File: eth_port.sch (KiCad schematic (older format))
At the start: 48 parts, among them J301 8P8C_LED_Shielded, U301 LAN8810

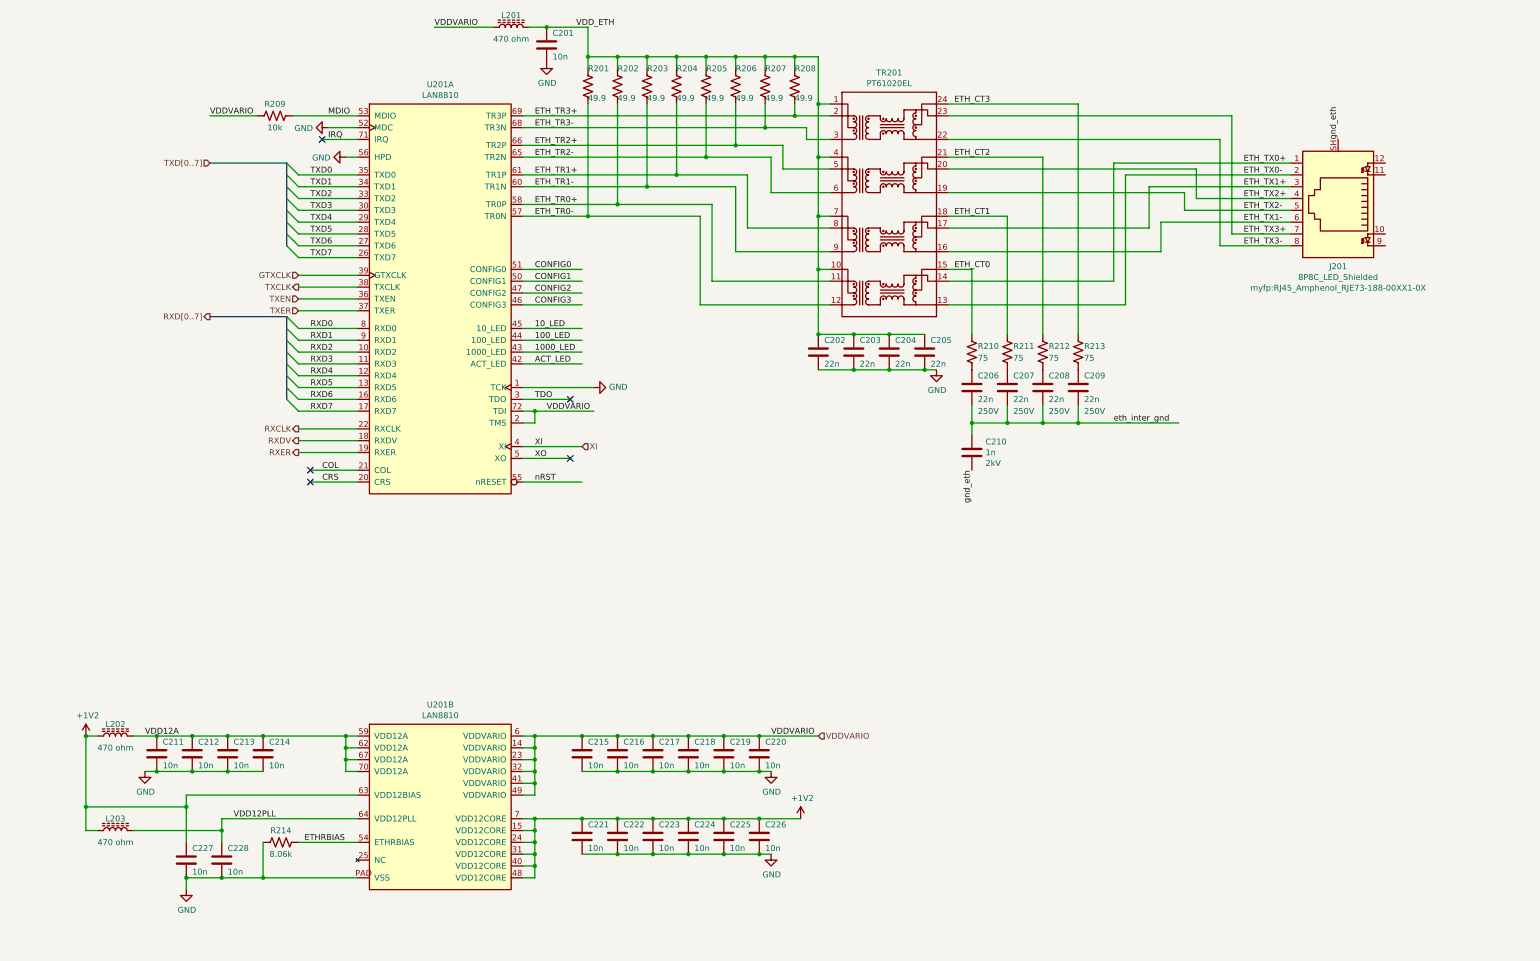
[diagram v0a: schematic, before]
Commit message: - Selected, schematic'd, placed & routed a crystal oscillator - Filled various internal planes to even out board thickness as well as   improve EMI performance - Added some identifying text to the top silkscreen
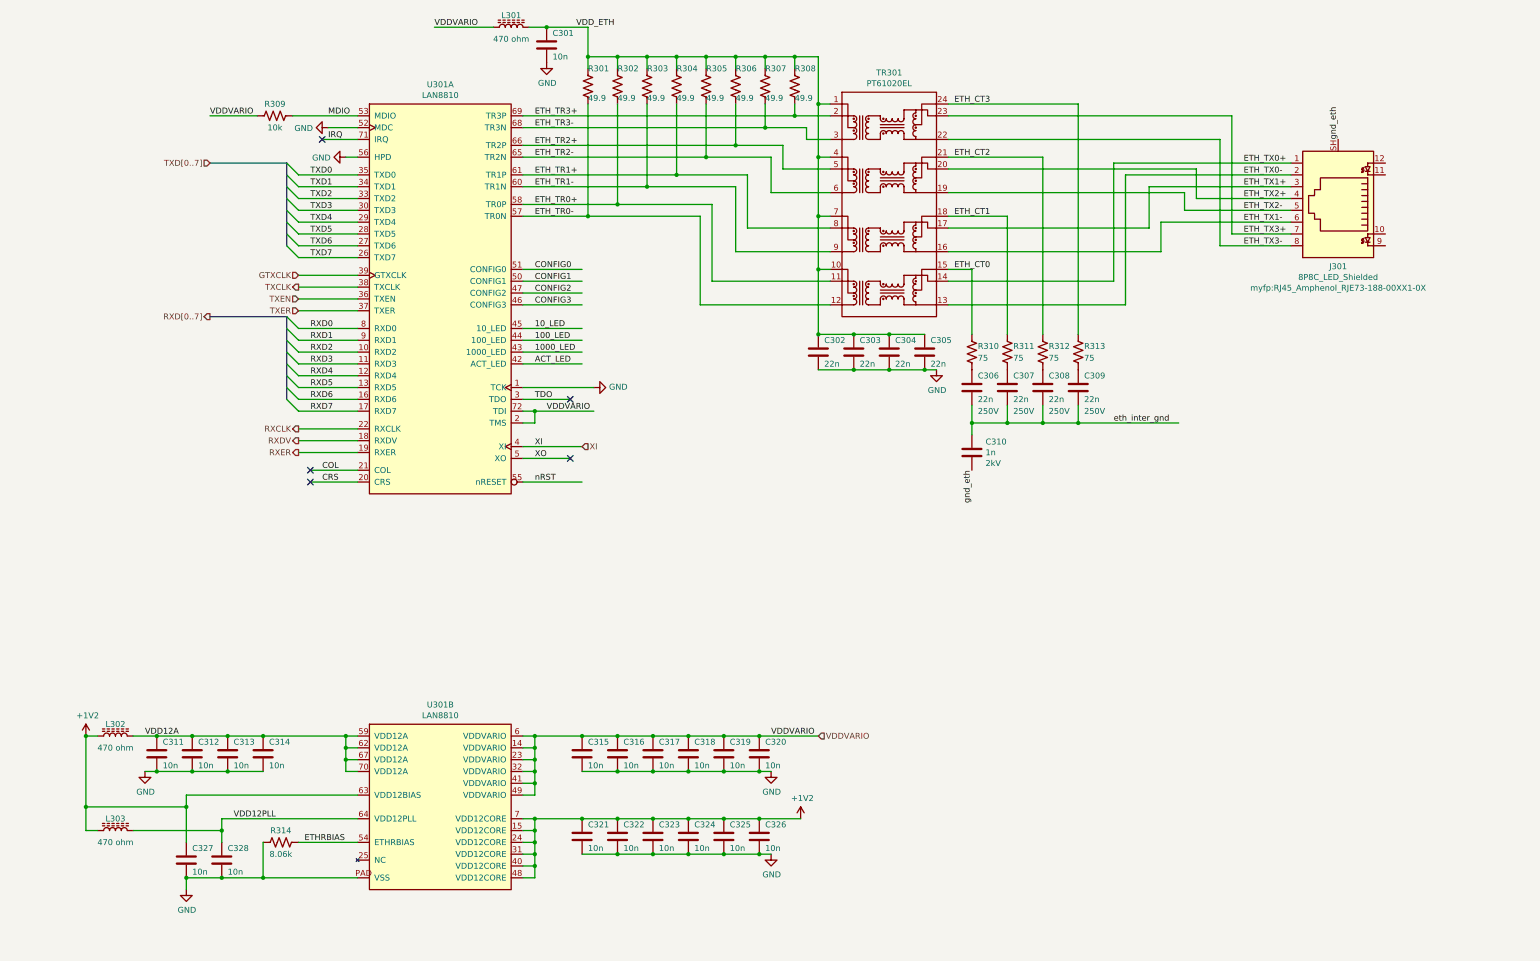
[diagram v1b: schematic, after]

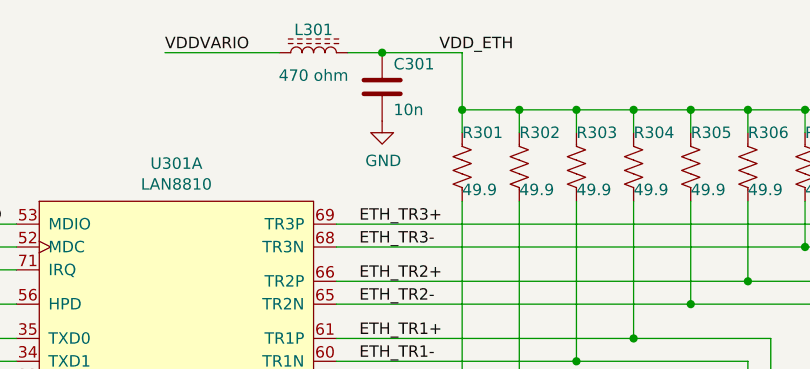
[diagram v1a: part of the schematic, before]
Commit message: - Removed C201/C301 which were the first two bypass caps on VCC_ETH - Placed last two components - Tweaked some planes, I think? - Finished routing all nets from the current schematic!!!
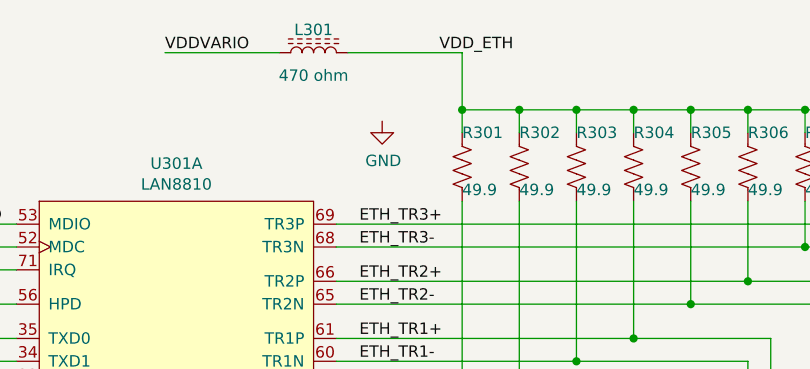
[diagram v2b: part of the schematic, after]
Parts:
- removed C301: 10n, Capacitor_SMD:C_0603_1608Metric, symbol Device:C
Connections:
- wire segments 244 -> 243
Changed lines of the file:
@@
 	0    -1   -1   0
 $EndComp
-$Comp
-L Device:C C301
-U 1 1 639B9E37
-P 5400 1100
-AR Path="/638EC3A5/639B9E37" Ref="C301"  Part="1"
-AR Path="/638E68FB/639B9E37" Ref="C201"  Part="1"
-F 0 "C301" H 5450 1200 50  0000 L CNN
-F 1 "10n" H 5450 1000 50  0000 L CNN
-F 2 "Capacitor_SMD:C_0603_1608Metric" H 5438 950 50  0001 C CNN
-F 3 "~" H 5400 1100 50  0001 C CNN
-F 4 "10V" H 5400 1100 50  0001 C CNN "Voltage"
-	1    5400 1100
-	1    0    0    -1
-$EndComp
-Wire Wire Line
-	5250 950  5400 950
 Connection ~ 5750 1200
 $Comp
@@
 Wire Wire Line
 	5750 950  5750 1200
-Connection ~ 5400 950
-Wire Wire Line
-	5400 950  5750 950
 NoConn ~ 5600 4600
 NoConn ~ 3400 4700
@@
 Wire Wire Line
 	5200 4100 5600 4100
+Text Label 5300 4100 0    50   ~ 0
+TDO
 Wire Bus Line
 	3200 3400 3200 4100
 Wire Bus Line
 	3200 2100 3200 2800
-Text Label 5300 4100 0    50   ~ 0
-TDO
+Wire Wire Line
+	5250 950  5750 950
 $EndSCHEMATC

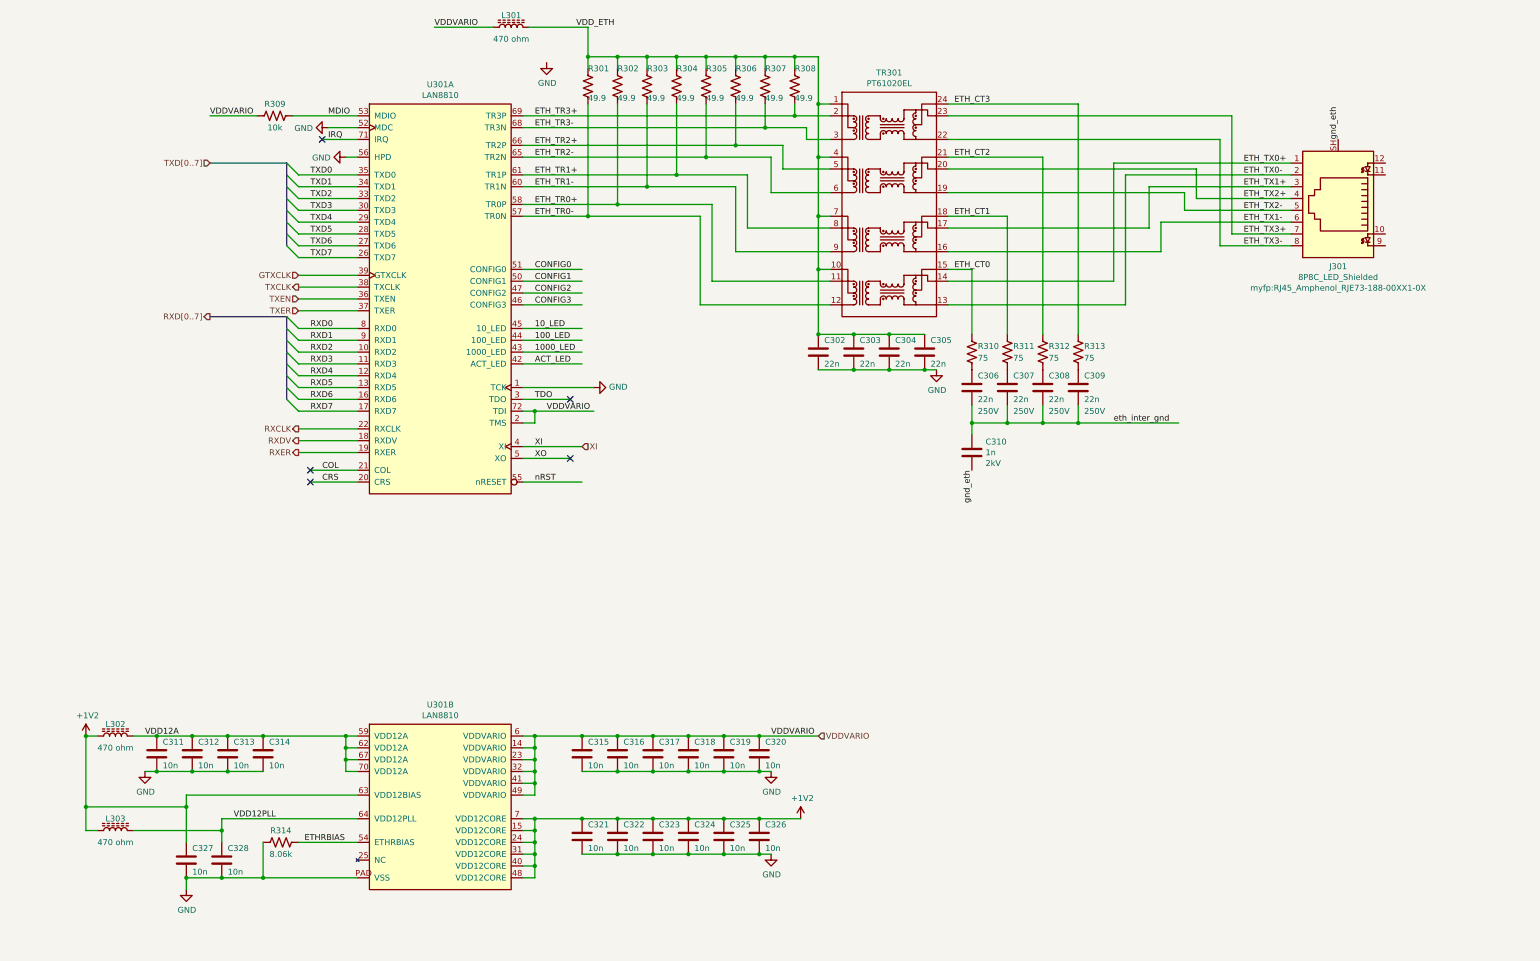
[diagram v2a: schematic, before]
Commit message: - Added HPD_MODE strap resistor - Narrowed down from an RJ45 family P/N to a very specific P/N - Added RJ45 LED hookups - Added CONFIG0/1/2/3 hookups, including a bunch of 0402 zero-ohm options - Placed and routed all of the above except the LED resistors/traces
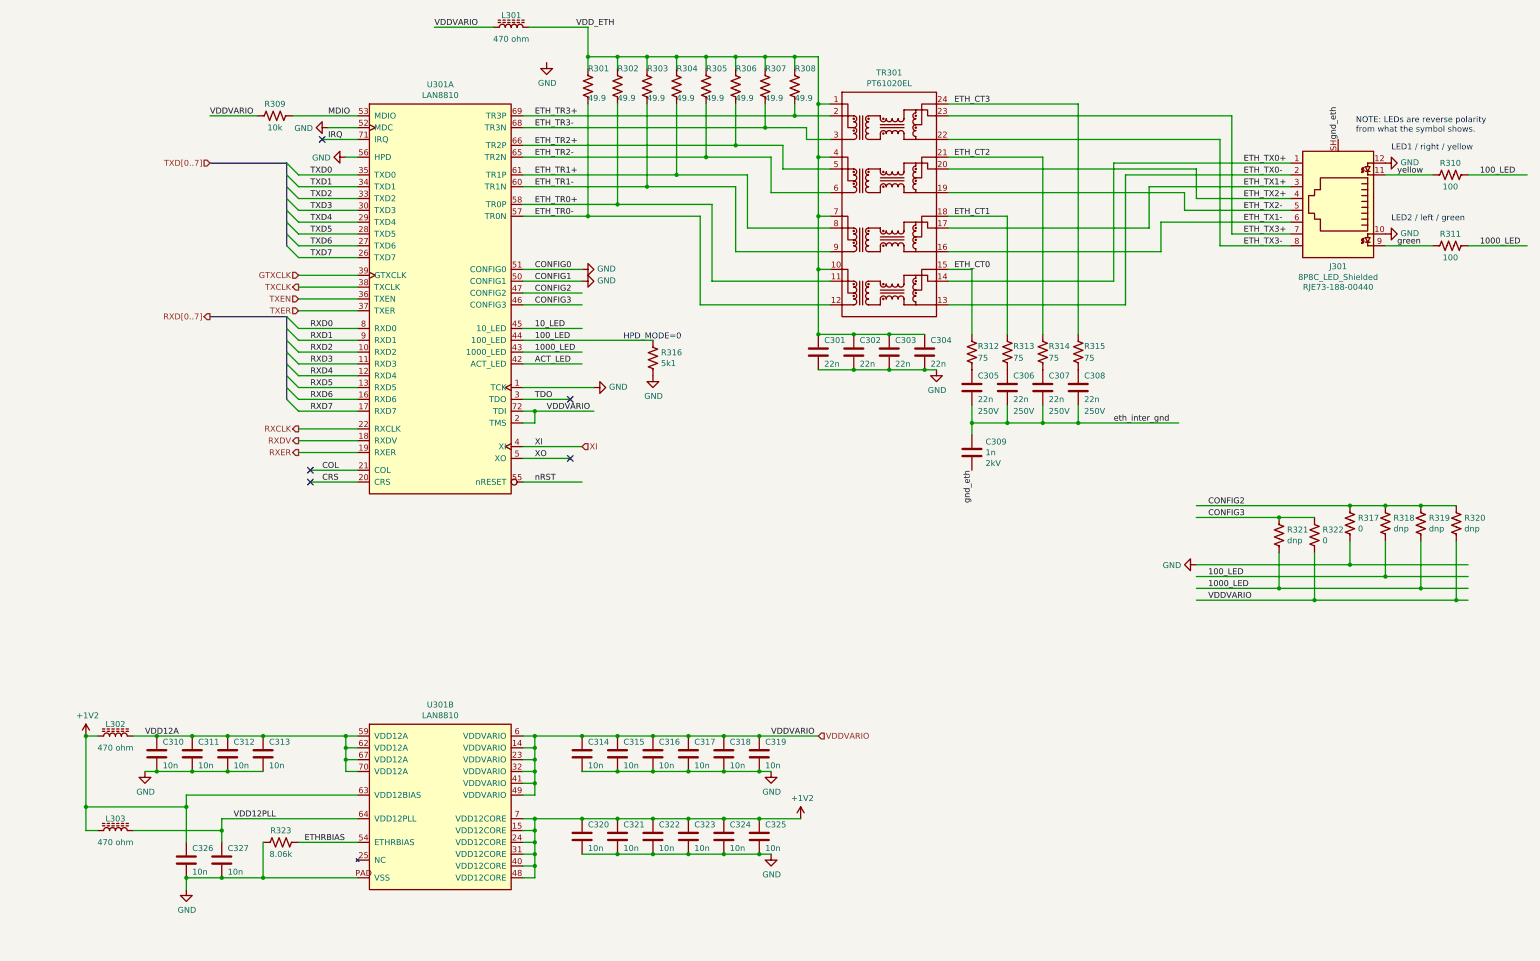
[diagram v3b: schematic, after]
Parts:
- added R210, R211: 100, Resistor_SMD:R_0603_1608Metric, symbol Device:R_US
- added R217, R222: 0, Resistor_SMD:R_0402_1005Metric, symbol Device:R_US
- added R218, R219, R220, R221: dnp, Resistor_SMD:R_0402_1005Metric, symbol Device:R_US
- added R316: 5k1, Resistor_SMD:R_0603_1608Metric, symbol Device:R_US
- J301: Part# (none) -> RJE73-188-00440
- renumbered C206 to C205, C207 to C206, C208 to C207, C209 to C208, C210 to C209, C302 to C301, C303 to C302, C304 to C303, C305 to C304, C311 to C310, C312 to C311, C313 to C312, C314 to C313, C315 to C314, C316 to C315, C317 to C316, C318 to C317, C319 to C318, C320 to C319, C321 to C320, C322 to C321, C323 to C322, C324 to C323, C325 to C324, C326 to C325, C327 to C326, C328 to C327, R210 to R212, R211 to R213, R212 to R214, R213 to R215, R314 to R323
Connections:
- net labels added: green, yellow
- wire segments 243 -> 269
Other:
- note added: "HPD_MODE=0"
- note added: "LED1 / right / yellow"
- note added: "LED2 / left / green"
- note added: "NOTE: LEDs are reverse polarity\nfrom what the symbol shows."

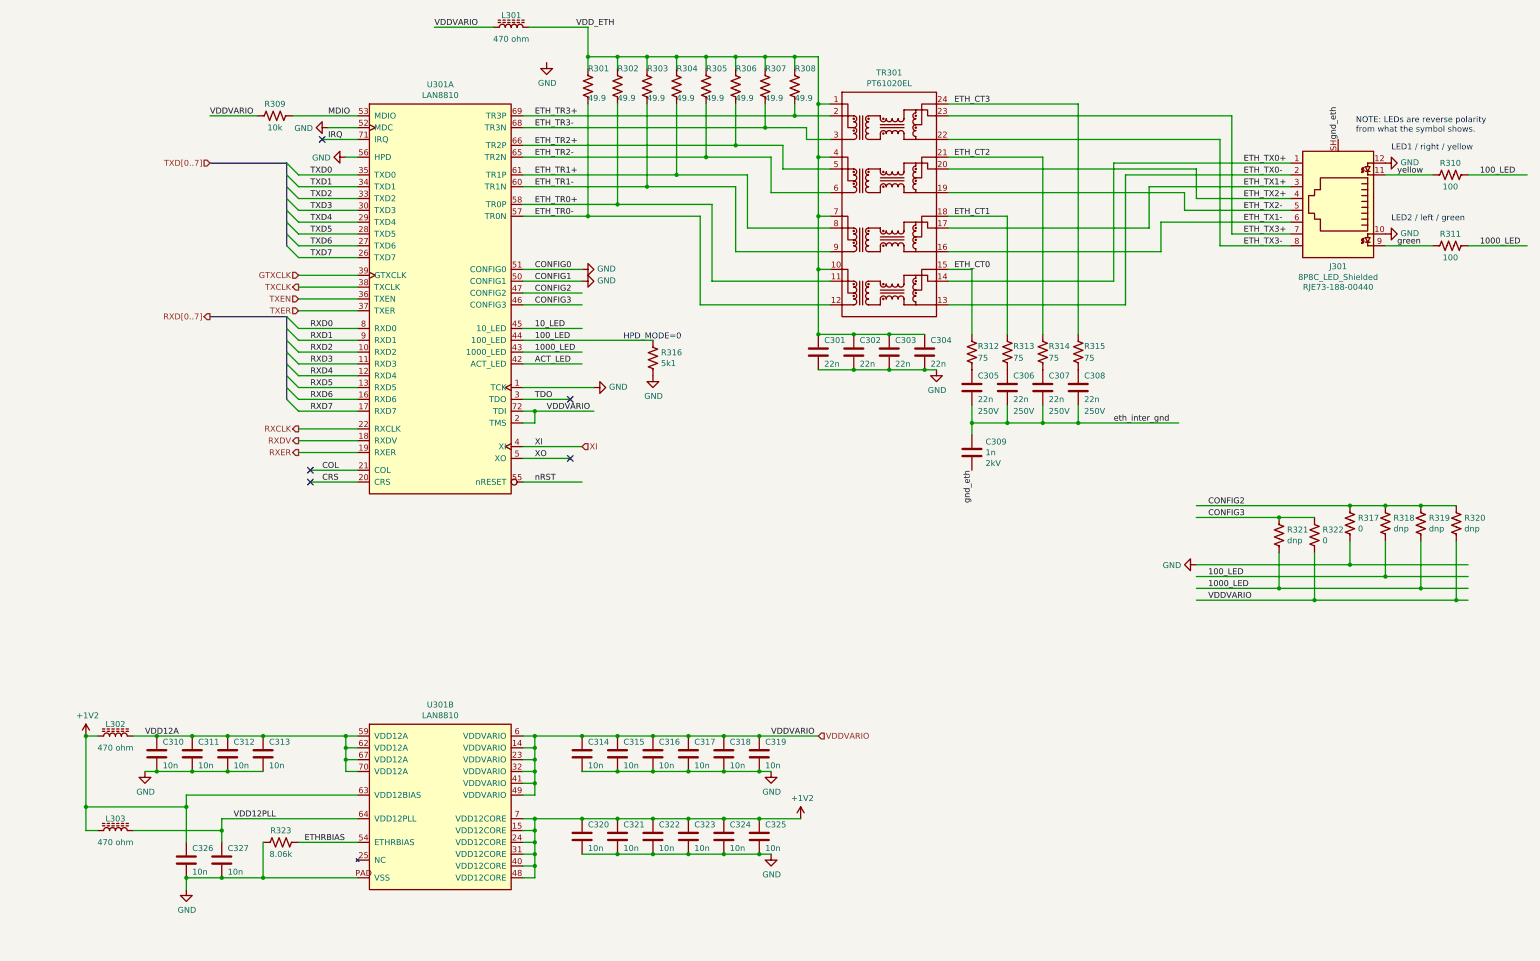
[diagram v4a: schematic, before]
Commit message: Added RC+D circuits for power-on reset of PHY chips.  Running out of room...
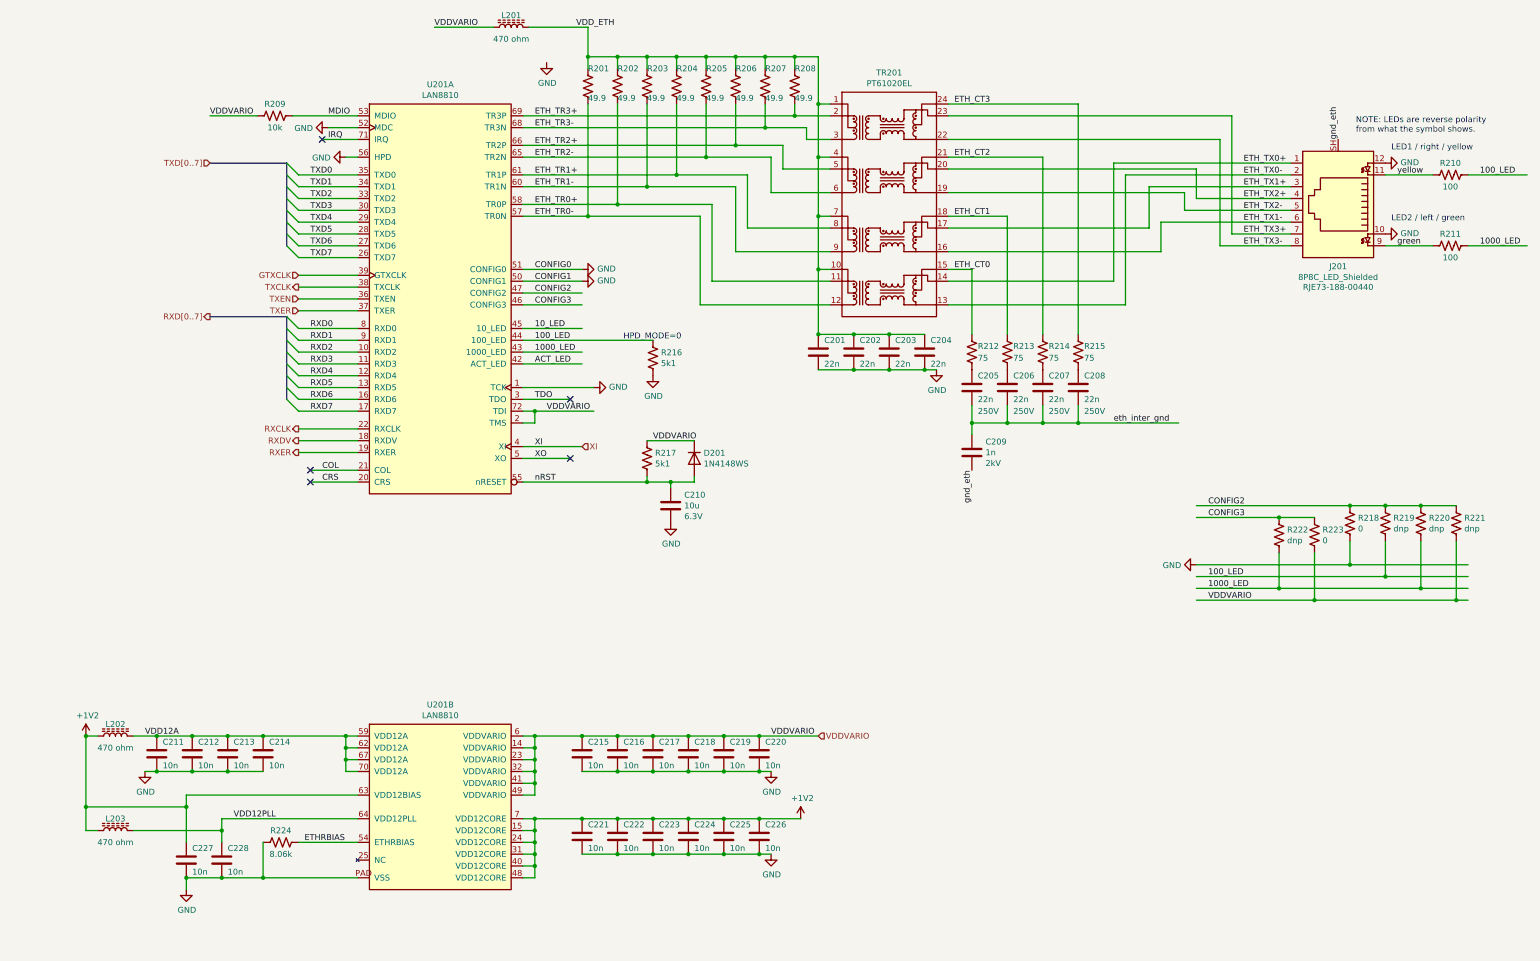
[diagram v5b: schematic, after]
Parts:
- added C210: 10u, Capacitor_SMD:C_0805_2012Metric, symbol Device:C
- added D201: 1N4148WS, Diode_SMD:D_SOD-323, symbol Device:D
- added R217: 5k1, Resistor_SMD:R_0603_1608Metric, symbol Device:R_US
- renumbered C310 to C311, C311 to C312, C312 to C313, C313 to C314, C314 to C315, C315 to C316, C316 to C317, C317 to C318, C318 to C319, C319 to C320, C320 to C321, C321 to C322, C322 to C323, C323 to C324, C324 to C325, C325 to C326, C326 to C327, C327 to C328, R217 to R218, R218 to R219, R219 to R220, R220 to R221, R221 to R222, R222 to R223, R323 to R324
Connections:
- wire segments 269 -> 275
